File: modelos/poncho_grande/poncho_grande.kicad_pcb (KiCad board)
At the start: 2 copper layers, 15 parts, among them K1 CONN_3, K2 CONN_3, P1 CONN_6, P10 CONN_4, P11 CONN_4, P12 CONN_5, P2 CONN_4, P3 CONN_5, P4 CONN_5, P5 CONN_4, P6 CONN_4, P7 CONN_5, P8 CONN_5, P9 CONN_6

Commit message: * Mejoras y emprolijamiento en el esquemático y el PCB.
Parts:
- removed K1, K2: CONN_3, Connect:bornier3
- added MP?: Plantilla, mod:plantilla, F.Cu at (138.4, 92.1)
- added P13: CONN_5, mod:bornier5, F.Cu at (154.3, 96.5)
- added P14: CONN_6, mod:bornier6, F.Cu at (68.6, 69.8)
- P1: footprint Connect:bornier6 -> mod:bornier6
- P10: value CONN_4 -> CONN_3; footprint Connect:bornier4 -> mod:bornier3
- P11, P5: value CONN_4 -> CONN_5; footprint Connect:bornier4 -> mod:bornier5
- P12, P3, P4: footprint Connect:bornier5 -> mod:bornier5
- P2: footprint Connect:bornier5 -> mod:bornier4
- P6: footprint Connect:bornier4 -> mod:bornier4
- P7: value CONN_5 -> CONN_4; footprint Connect:bornier5 -> mod:bornier4
- P8: value CONN_5 -> CONN_3; footprint Connect:bornier5 -> mod:bornier3
- P9: value CONN_6 -> CONN_4; footprint Connect:bornier6 -> mod:bornier4
- moved P2 111.5 mm to (154.9, 148.0), turned to 270 degrees
- moved P5 74.1 mm to (85.7, 123.8), turned to 90 degrees
- moved P10 71.2 mm to (83.8, 49.5), turned to 180 degrees
- moved P1 54.7 mm to (91.4, 64.8)
- moved P7 50.9 mm to (102.9, 101.0)
- moved P3 50.4 mm to (121.3, 97.8), turned to 270 degrees
- moved P8 45.1 mm to (102.9, 118.7)
- moved P9 44.7 mm to (101.6, 49.5), turned to 180 degrees
- moved P11 41.3 mm to (154.3, 123.2)
- moved P6 32.5 mm to (85.7, 101.0)
- moved P12 26.7 mm to (129.5, 49.5), turned to 180 degrees
- moved XA1 24.3 mm to (138.4, 92.1)
- moved P4 24.0 mm to (121.3, 123.2)
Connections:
- P1 pad 1: +3V3 -> +3.3V
- P10 pad 1: /Circuito Principal/RESET -> /Circuito Principal/GPIO7
- P10 pad 2: /Circuito Principal/ISP -> /Circuito Principal/GPIO8
- P10 pad 3: /Circuito Principal/WAKEUP -> GND
- P11 pad 1: +5P -> +5V
- P11 pad 2: /Circuito Principal/GPIO4 -> +3.3V
- P11 pad 3: /Circuito Principal/GPIO5 -> /Circuito Principal/RD
- P11 pad 4: /Circuito Principal/GPIO6 -> /Circuito Principal/TD
- P12 pad 1: +5P -> +5V
- P12 pad 2: +3.3VP -> +3.3V
- P12 pad 3: /Circuito Principal/LCD1 -> /Circuito Principal/SDA
- P12 pad 4: /Circuito Principal/LCD2 -> /Conector del Poncho/SCL
- P12 pad 5: /Circuito Principal/LCD3 -> GND
- P2 pad 1: +5V -> /Circuito Principal/RESET
- P2 pad 2: +3V3 -> /Circuito Principal/ISP
- P2 pad 3: /Circuito Principal/RXD -> /Circuito Principal/WAKEUP
- P2 pad 4: /Circuito Principal/TXD -> GND
- P3 pad 2: +3V3 -> +3.3V
- P5 pad 1: /Circuito Principal/LCD4 -> +5VP
- P5 pad 2: /Circuito Principal/LCD_EN -> +3.3VP
- P5 pad 3: /Circuito Principal/RS -> /Circuito Principal/LCD1
- P5 pad 4: GND -> /Circuito Principal/LCD2
- P6 pad 1: +5P -> /Circuito Principal/LCD4
- P6 pad 2: +3.3VP -> /Circuito Principal/LCD_EN
- P6 pad 3: /Circuito Principal/GPIO0 -> /Circuito Principal/RS
- P6 pad 4: /Circuito Principal/GPIO0 -> GND
- P7 pad 1: +5V -> +5VP
- P7 pad 2: +3V3 -> +3.3VP
- P7 pad 3: /Circuito Principal/RD -> /Circuito Principal/GPIO0
- P7 pad 4: /Circuito Principal/TD -> /Circuito Principal/GPIO1
- P8 pad 1: +5V -> /Circuito Principal/GPIO2
- P8 pad 2: +3V3 -> /Circuito Principal/GPIO3
- P8 pad 3: /Circuito Principal/SDA -> GND
- P9 pad 1: +5P -> +5VP
- P9 pad 2: +3.3VP -> /Circuito Principal/GPIO4
- P9 pad 3: /Circuito Principal/spiCCK -> /Circuito Principal/GPIO5
- P9 pad 4: /Circuito Principal/MOSI -> /Circuito Principal/GPIO6
- XA1 pad 1: +3V3 -> +3.3V
- XA1 pad 17: +3.3VADC -> (no net)
- XA1 pad 42: +5P -> +5VP
- XA1 pad 44: /Circuito Principal/RXD1 -> (no net)
- XA1 pad 46: /Circuito Principal/TXEN -> (no net)
- XA1 pad 48: /Circuito Principal/MDC -> (no net)
- XA1 pad 49: /Circuito Principal/RXD0 -> (no net)
- XA1 pad 50: /Circuito Principal/CRS -> (no net)
- XA1 pad 52: /Circuito Principal/MDIO -> (no net)
- XA1 pad 54: /Circuito Principal/TXD0 -> (no net)
- XA1 pad 55: /Circuito Principal/RCLK -> (no net)
- XA1 pad 56: /Circuito Principal/TXD1 -> (no net)
- XA1 pad 72: /Circuito Principal/GPIO0 -> /Circuito Principal/GPIO1

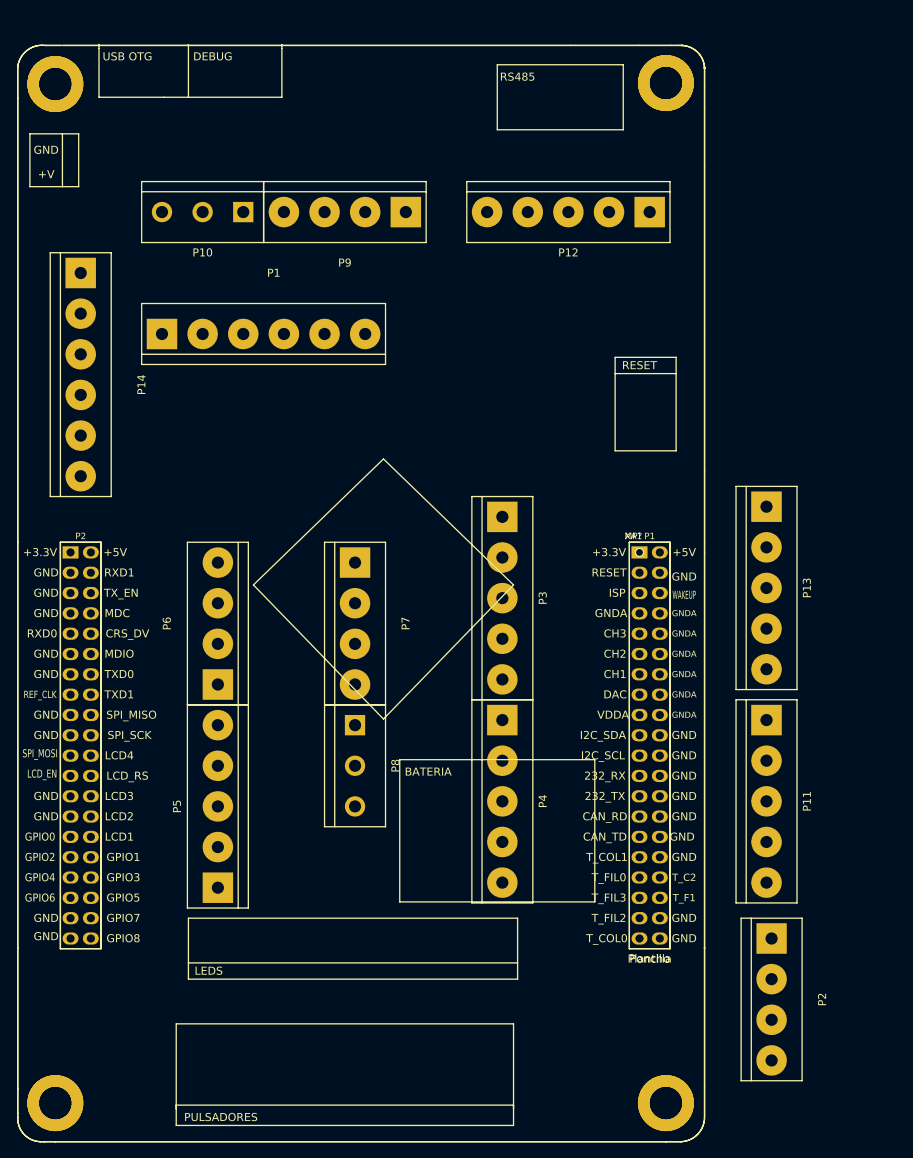
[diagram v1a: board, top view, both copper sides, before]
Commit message: * Ruteo del Poncho ejemplo con área de prototipado.
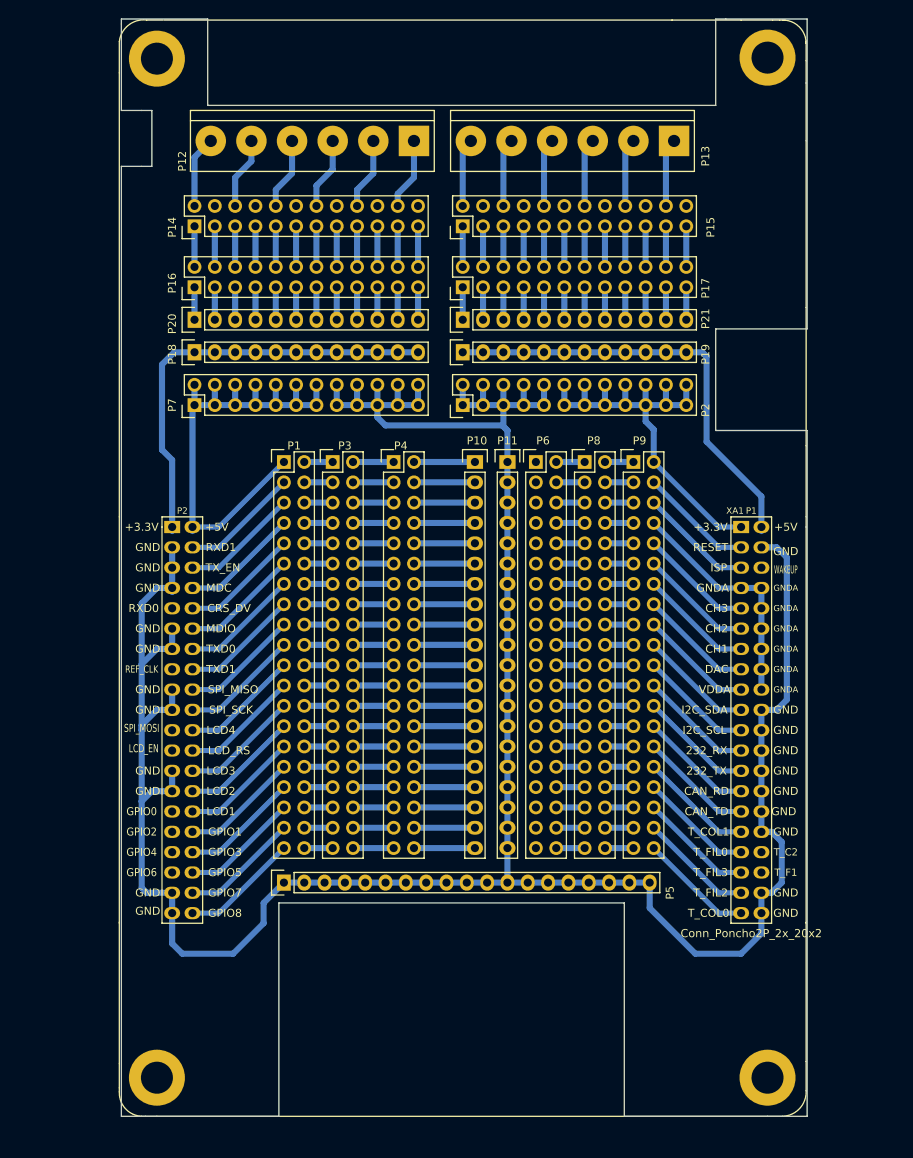
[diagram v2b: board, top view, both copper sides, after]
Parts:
- removed MP?: Plantilla, mod:plantilla
- added P15: CONN_02X12, Pin_Headers:Pin_Header_Straight_2x12, F.Cu at (116.3, 51.3)
- added P16: CONN_02X12, Pin_Headers:Pin_Header_Straight_2x12, F.Cu at (82.8, 58.9)
- added P17: CONN_02X12, Pin_Headers:Pin_Header_Straight_2x12, F.Cu at (116.3, 58.9)
- added P18: CONN_01X12, Pin_Headers:Pin_Header_Straight_1x12, F.Cu at (82.8, 67.1)
- added P19: CONN_01X12, Pin_Headers:Pin_Header_Straight_1x12, F.Cu at (116.3, 67.1)
- added P20: CONN_01X12, Pin_Headers:Pin_Header_Straight_1x12, F.Cu at (82.8, 63.0)
- added P21: CONN_01X12, Pin_Headers:Pin_Header_Straight_1x12, F.Cu at (116.3, 63.0)
- P1: value CONN_6 -> CONN_02X20; footprint mod:bornier6 -> Pin_Headers:Pin_Header_Straight_2x20
- P10: value CONN_3 -> CONN_01X20; footprint mod:bornier3 -> Pin_Headers:Pin_Header_Straight_1x20
- P11: value CONN_5 -> CONN_01X20; footprint mod:bornier5 -> Pin_Headers:Pin_Header_Straight_1x20
- P12, P13: value CONN_5 -> CONN_01X06; footprint mod:bornier5 -> mod:bornier6
- P14: value CONN_6 -> CONN_02X12; footprint mod:bornier6 -> Pin_Headers:Pin_Header_Straight_2x12
- P2, P7: value CONN_4 -> CONN_01X20; footprint mod:bornier4 -> Pin_Headers:Pin_Header_Straight_2x12
- P3, P4: value CONN_5 -> CONN_02X20; footprint mod:bornier5 -> Pin_Headers:Pin_Header_Straight_2x20
- P5: value CONN_5 -> CONN_01X40; footprint mod:bornier5 -> Pin_Headers:Pin_Header_Straight_1x19
- P6, P9: value CONN_4 -> CONN_02X20; footprint mod:bornier4 -> Pin_Headers:Pin_Header_Straight_2x20
- P8: value CONN_3 -> CONN_02X20; footprint mod:bornier3 -> Pin_Headers:Pin_Header_Straight_2x20
- XA1: value Poncho -> Conn_Poncho2P_2x_20x2
- moved P2 83.7 mm to (116.3, 73.7), turned to 90 degrees
- moved P13 60.9 mm to (130.0, 40.6), turned to 180 degrees
- moved P11 53.4 mm to (121.9, 80.8), turned to 0 degrees
- moved P9 47.7 mm to (137.7, 80.8), turned to 0 degrees
- moved P8 47.6 mm to (131.6, 80.8), turned to 0 degrees
- moved P10 46.2 mm to (117.9, 80.8), turned to 0 degrees
- moved P6 44.6 mm to (125.5, 80.8), turned to 0 degrees
- moved P4 44.5 mm to (107.7, 80.8), turned to 0 degrees
- moved P7 33.9 mm to (82.8, 73.7), turned to 90 degrees
- moved P12 33.2 mm to (97.5, 40.6)
- moved P3 27.2 mm to (100.1, 80.8), turned to 0 degrees
- moved P14 23.4 mm to (82.8, 51.3), turned to 90 degrees
- moved P1 16.2 mm to (94.0, 80.8)
- moved XA1 13.1 mm to (151.1, 88.9)
- moved P5 12.6 mm to (94.0, 133.3)
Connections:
- P1 pad 1: +3.3V -> +5VP
- P1 pad 2: /Circuito Principal/ADC1 -> Net-(P1-Pad2)
- P1 pad 3: /Circuito Principal/ADC2 -> /Circuito Principal/RXD1
- P1 pad 4: /Circuito Principal/ADC3 -> Net-(P1-Pad4)
- P1 pad 5: /Circuito Principal/DAC -> /Circuito Principal/TXEN
- P1 pad 6: GNDA -> Net-(P1-Pad6)
- P10 pad 1: /Circuito Principal/GPIO7 -> Net-(P10-Pad1)
- P10 pad 2: /Circuito Principal/GPIO8 -> Net-(P10-Pad2)
- P10 pad 3: GND -> Net-(P10-Pad3)
- P11 pad 1: +5V -> GND
- P11 pad 2: +3.3V -> GND
- P11 pad 3: /Circuito Principal/RD -> GND
- P11 pad 4: /Circuito Principal/TD -> GND
- P12 pad 1: +5V -> Net-(P12-Pad1)
- P12 pad 2: +3.3V -> Net-(P12-Pad2)
- P12 pad 3: /Circuito Principal/SDA -> Net-(P12-Pad3)
- P12 pad 4: /Conector del Poncho/SCL -> Net-(P12-Pad4)
- P12 pad 5: GND -> Net-(P12-Pad5)
- P13 pad 1: +5V -> Net-(P13-Pad1)
- P13 pad 2: +3.3V -> Net-(P13-Pad2)
- P13 pad 3: /Circuito Principal/RXD -> Net-(P13-Pad3)
- P13 pad 4: /Circuito Principal/TXD -> Net-(P13-Pad4)
- P13 pad 5: GND -> Net-(P13-Pad5)
- P14 pad 1: +5VP -> Net-(P14-Pad1)
- P14 pad 2: +3.3VP -> Net-(P12-Pad6)
- P14 pad 3: /Circuito Principal/spiCCK -> Net-(P14-Pad3)
- P14 pad 4: /Circuito Principal/MOSI -> (no net)
- P14 pad 5: /Circuito Principal/MISO -> Net-(P14-Pad5)
- P14 pad 6: GND -> Net-(P12-Pad5)
- P2 pad 1: /Circuito Principal/RESET -> GND
- P2 pad 2: /Circuito Principal/ISP -> GND
- P2 pad 3: /Circuito Principal/WAKEUP -> GND
- P3 pad 1: +5V -> Net-(P1-Pad2)
- P3 pad 2: +3.3V -> Net-(P3-Pad2)
- P3 pad 3: /Circuito Principal/COL0 -> Net-(P1-Pad4)
- P3 pad 4: /Circuito Principal/COL1 -> Net-(P3-Pad4)
- P3 pad 5: /Circuito Principal/COL2 -> Net-(P1-Pad6)
- P4 pad 1: /Circuito Principal/F0 -> Net-(P3-Pad2)
- P4 pad 2: /Circuito Principal/F1 -> Net-(P10-Pad1)
- P4 pad 3: /Circuito Principal/F2 -> Net-(P3-Pad4)
- P4 pad 4: /Circuito Principal/F3 -> Net-(P10-Pad2)
- P4 pad 5: GND -> Net-(P3-Pad6)
- P5 pad 1: +5VP -> GND
- P5 pad 2: +3.3VP -> GND
- P5 pad 3: /Circuito Principal/LCD1 -> GND
- P5 pad 4: /Circuito Principal/LCD2 -> GND
- P5 pad 5: /Circuito Principal/LCD3 -> GND
- P6 pad 1: /Circuito Principal/LCD4 -> (no net)
- P6 pad 2: /Circuito Principal/LCD_EN -> Net-(P6-Pad2)
- P6 pad 3: /Circuito Principal/RS -> (no net)
- P6 pad 4: GND -> Net-(P6-Pad4)
- P7 pad 2: +3.3VP -> +5VP
- P7 pad 3: /Circuito Principal/GPIO0 -> +5VP
- P7 pad 4: /Circuito Principal/GPIO1 -> +5VP
- P8 pad 1: /Circuito Principal/GPIO2 -> Net-(P6-Pad2)
- P8 pad 2: /Circuito Principal/GPIO3 -> Net-(P8-Pad2)
- P8 pad 3: GND -> Net-(P6-Pad4)
- P9 pad 1: +5VP -> Net-(P8-Pad2)
- P9 pad 2: /Circuito Principal/GPIO4 -> +3.3V
- P9 pad 3: /Circuito Principal/GPIO5 -> Net-(P8-Pad4)
- P9 pad 4: /Circuito Principal/GPIO6 -> /Circuito Principal/RESET
- XA1 pad 17: (no net) -> +3.3VADC
- XA1 pad 21: /Conector del Poncho/SCL -> /Circuito Principal/SCL
- XA1 pad 34: /Circuito Principal/COL2 -> (no net)
- XA1 pad 36: /Circuito Principal/F1 -> (no net)
- XA1 pad 44: (no net) -> /Circuito Principal/RXD1
- XA1 pad 46: (no net) -> /Circuito Principal/TXEN
- XA1 pad 48: (no net) -> /Circuito Principal/MDC
- XA1 pad 50: (no net) -> /Circuito Principal/CRS
- XA1 pad 52: (no net) -> /Circuito Principal/MDIO
- XA1 pad 54: (no net) -> /Circuito Principal/TXD0
- XA1 pad 56: (no net) -> /Circuito Principal/TXD1
- XA1 pad 6: /Circuito Principal/WAKEUP -> (no net)
- XA1 pad 61: /Circuito Principal/MOSI -> (no net)
- XA1 pad 63: /Circuito Principal/LCD_EN -> (no net)
- XA1 pad 69: /Circuito Principal/GPIO0 -> (no net)
- XA1 pad 71: /Circuito Principal/GPIO2 -> (no net)
- XA1 pad 73: /Circuito Principal/GPIO4 -> (no net)
- XA1 pad 75: /Circuito Principal/GPIO6 -> (no net)
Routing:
- net GND: track 0.00 -> 343.7 mm
- net +5VP: track 0.00 -> 64.0 mm
- net +5V: track 0.00 -> 55.4 mm
- net +3.3V: track 0.00 -> 54.8 mm
- net +3.3VP: track 0.00 -> 54.0 mm
- net GNDA: track 0.00 -> 29.5 mm
- net /Circuito Principal/GPIO5: track 0.00 -> 14.8 mm
- net /Circuito Principal/spiCCK: track 0.00 -> 14.8 mm
- net /Circuito Principal/TXEN: track 0.00 -> 14.8 mm
- net /Circuito Principal/TXD1: track 0.00 -> 14.8 mm
- net /Circuito Principal/TXD0: track 0.00 -> 14.8 mm
- net /Circuito Principal/RXD1: track 0.00 -> 14.8 mm
- net /Circuito Principal/RS: track 0.00 -> 14.8 mm
- net /Circuito Principal/MISO: track 0.00 -> 14.8 mm
- net /Circuito Principal/MDIO: track 0.00 -> 14.8 mm
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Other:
- board outline added: 85.7 x 137.2 mm
- net class Default: clearance 0.2 -> 0.508; trace_width 0.25 -> 0.381
- rule trace_clearance: 0.2 -> 0.508

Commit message: * Actualizado el modelo de Poncho Grande. Ya terminado de rutear.
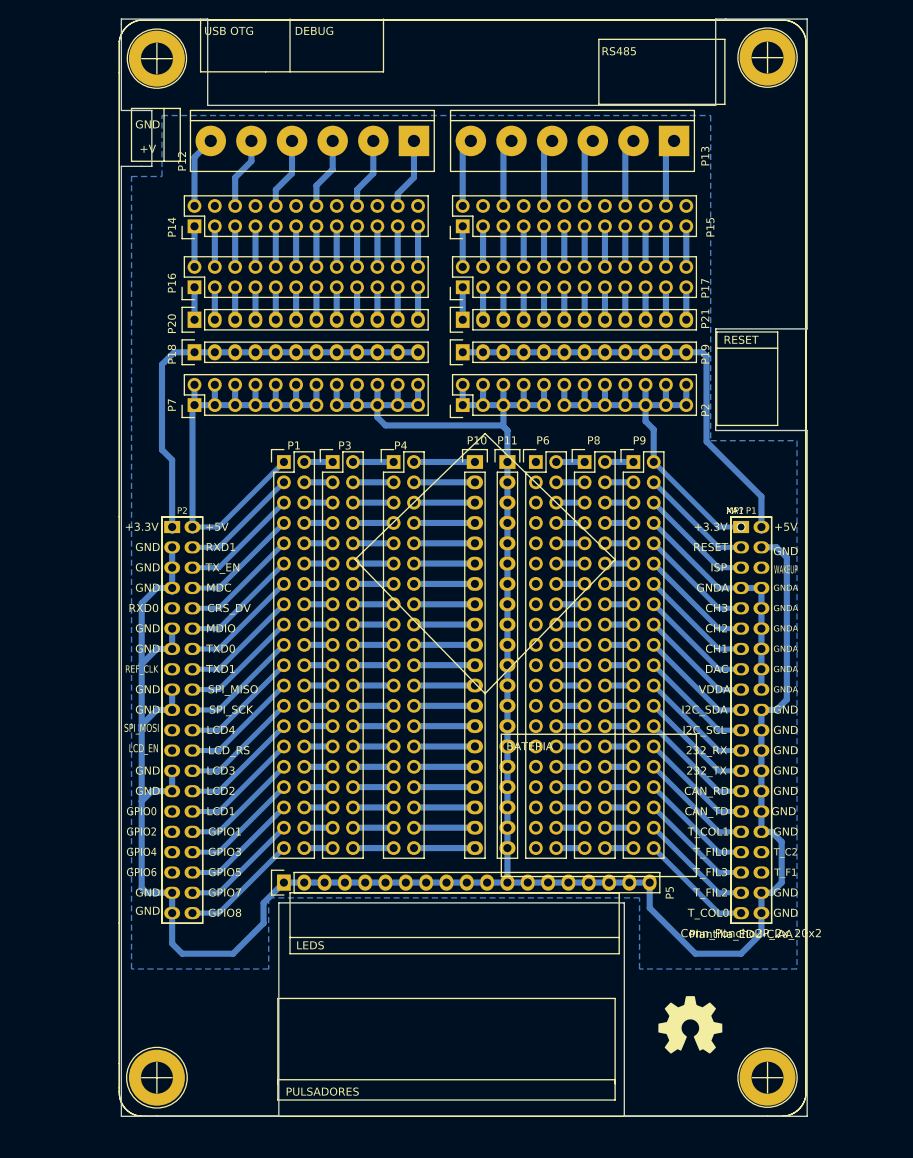
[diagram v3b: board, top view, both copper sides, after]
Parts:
- added G101: Logo_OSHWA, Poncho_Esqueleto:Logo_OSHWA, F.Cu at (144.8, 151.1)
- added MP?: Plantilla_EDU-CIAA, Poncho_Esqueleto:Plantilla_EDU-CIAA, F.Cu at (151.1, 88.9)
- P5: value CONN_01X40 -> CONN_01X19
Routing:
- added copper zone on B.Cu, net GND

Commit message: * Agrego logos y quito plantilla al poncho_grande.
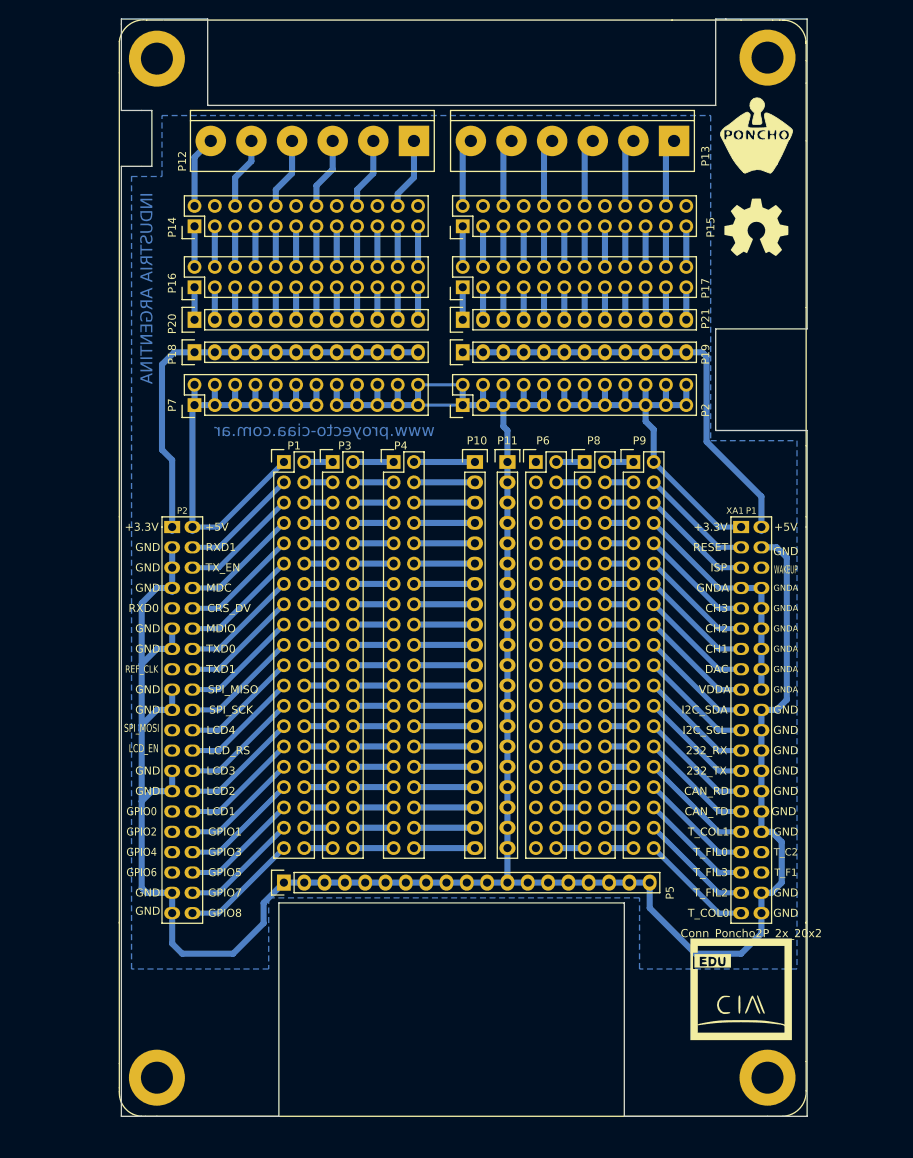
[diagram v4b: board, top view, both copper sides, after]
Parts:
- removed MP?: Plantilla_EDU-CIAA, Poncho_Esqueleto:Plantilla_EDU-CIAA
- added G***: LOGO, Poncho_Esqueleto:Logo_Poncho, F.Cu at (153.0, 40.0)
- added G***: Logo_EDU-CIAA, Poncho_Esqueleto:Logo_EDU-CIAA, F.Cu at (151.1, 146.7)
- moved G101 100.0 mm to (153.0, 51.4)
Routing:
- net GND: track 343.7 -> 336.4 mm
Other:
- board text added: "INDUSTRIA ARGENTINA"
- board text added: "www.proyecto-ciaa.com.ar"

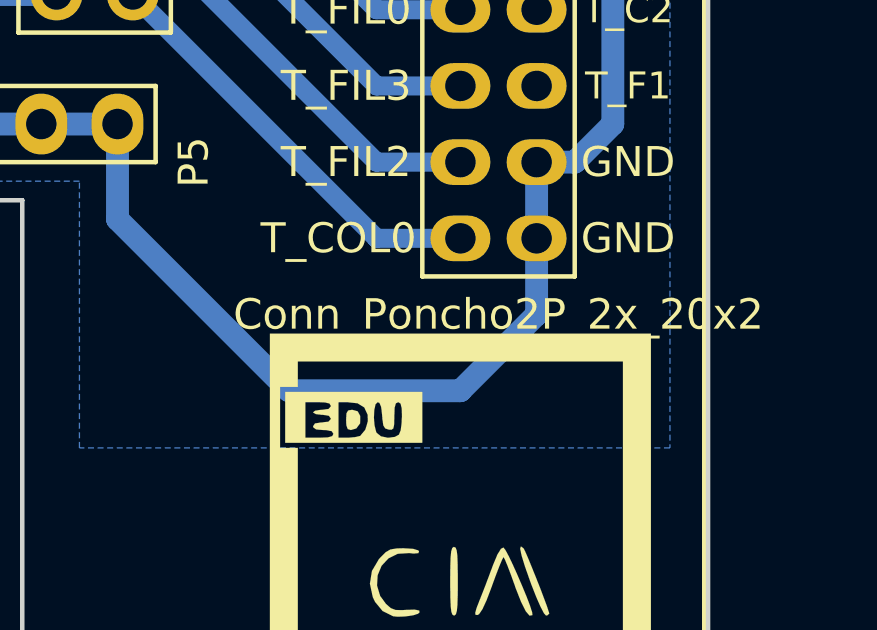
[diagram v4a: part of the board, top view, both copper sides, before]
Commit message: * Agregadas anotaciones y detalles.
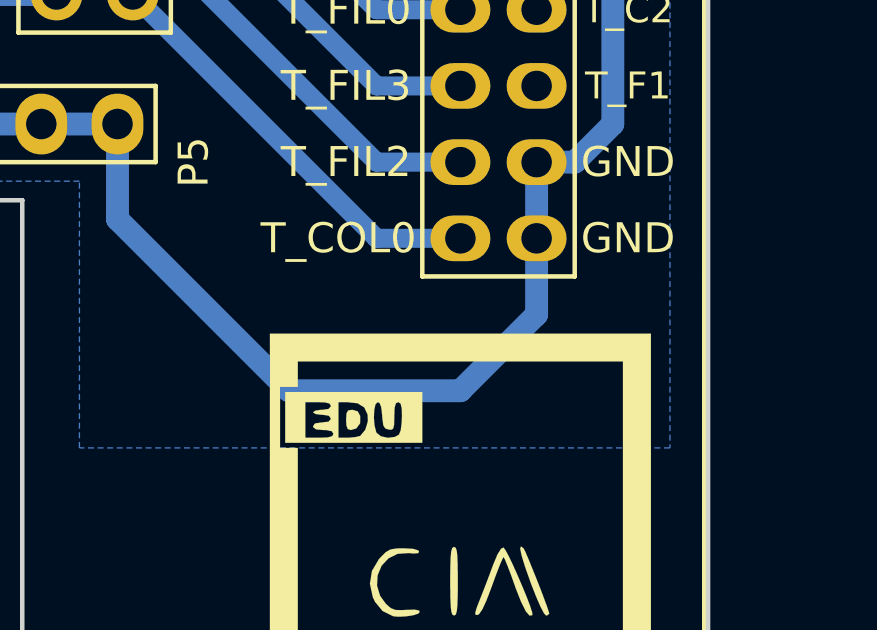
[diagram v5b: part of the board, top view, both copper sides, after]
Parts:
- XA1: value Conn_Poncho2P_2x_20x2 -> (none)
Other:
- board text added: "PENDIENTES: * Colocar serigrafía para indicar señales y alimentaciones en el área de prototipado."
